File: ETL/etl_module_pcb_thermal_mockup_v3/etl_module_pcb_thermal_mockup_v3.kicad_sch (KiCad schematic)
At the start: 11 parts, among them J1 WP7B-S050VA1-R8000, J2 WP7B-S050VA1-R8000, J3 Conn_02x02_Odd_Even, J4 Conn_02x08_Counter_Clockwise, J5 Conn_02x08_Counter_Clockwise, J6 Conn_02x08_Counter_Clockwise, J7 Conn_02x08_Counter_Clockwise, X1 ETROC_dummy_thermal_sensors, X2 ETROC_dummy_thermal_sensors, X3 ETROC_dummy_thermal_sensors, X4 ETROC_dummy_thermal_sensors

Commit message: Progress on etl_module_pcb_thermal_mcokup_v3
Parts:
- J4, J5, J6, J7: symbol Connector_Generic:Conn_02x08_Counter_Clockwise -> Connector_Generic:Conn_02x08_Odd_Even
- U2: renamed from X2; footprint unl_silab:PCB_ETROC2_dummy -> (none)
- U3: renamed from X3; footprint unl_silab:PCB_ETROC2_dummy -> (none)
- U4: renamed from X4; footprint unl_silab:PCB_ETROC2_dummy -> (none)
- renumbered X1 to U1
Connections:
- net X1EBR2: now reaches J4.1 (Pin_1)
- net X1EBR2: now also U1.119 (ETROC_BR-)
- net X1LBL1: now reaches J4.10 (Pin_10)
- net X1LBL1: now also U1.11 (LGAD_BL+)
- net X1LBR1: now reaches J4.11 (Pin_11)
- net X1LBR1: now also U1.104 (LGAD_BR+)
- net X1LBL2: now reaches J4.12 (Pin_12)
- net X1LBL2: now also U1.12 (LGAD_BL-)
- net X1LTR2: now reaches J4.13 (Pin_13)
- net X1LTR2: now also U1.83 (LGAD_TR-)
- net X1LTL1: now reaches J4.14 (Pin_14)
- net X1LTL1: now also U1.21 (LGAD_TL+)
- net X1LTR1: now reaches J4.15 (Pin_15)
- net X1LTR1: now also U1.81 (LGAD_TR+)
- net X1LTL2: now reaches J4.16 (Pin_16)
- net X1LTL2: now also U1.23 (LGAD_TL-)
- net X1EBL1: now reaches J4.2 (Pin_2)
- net X1EBL1: now also U1.3 (ETROC_BLp)
- net X1EBR1: now reaches J4.3 (Pin_3)
- net X1EBR1: now also U1.117 (ETROC_BR+)
- net X1EBL2: now reaches J4.4 (Pin_4)
- net X1EBL2: now also U1.5 (ETROC_BL-)
- net X1ETR2: now reaches J4.5 (Pin_5)
- net X1ETR2: now also U1.108 (ETROC_TR-)
- net X1ETL1: now reaches J4.6 (Pin_6)
- net X1ETL1: now also U1.8 (ETROC_TL+)
- net X1ETR1: now reaches J4.7 (Pin_7)
- net X1ETR1: now also U1.107 (ETROC_TR+)
- net X1ETL2: now reaches J4.8 (Pin_8)
- net X1ETL2: now also U1.9 (ETROC_TL-)
- net X1LBR2: now reaches J4.9 (Pin_9)
- net X1LBR2: now also U1.105 (LGAD_BR-)
- net 01_N: no longer names the net of J2.1
- net 01_P: no longer names the net of J2.2
- net 02_N: no longer names the net of J2.3
- net 02_P: no longer names the net of J2.4
- net 03_N: no longer names the net of J2.5
- net 03_P: no longer names the net of J2.6
- net 04_N: no longer names the net of J2.7
- net 04_P: no longer names the net of J2.8
- net 05_N: no longer names the net of J2.9
- net 05_P: no longer names the net of J2.10
- net 06_N: no longer names the net of J2.11
- net 06_P: no longer names the net of J2.12
- net 07_N: no longer names the net of J2.13
- net 07_P: no longer names the net of J2.14
- net 08_N: no longer names the net of J2.15
- net 08_P: no longer names the net of J2.16
- net 09_N: no longer names the net of J2.17
- net 09_P: no longer names the net of J2.18
- net 10_N: no longer names the net of J2.19
- net 10_P: no longer names the net of J2.20
- net 11_N: no longer names the net of J2.21
- net 11_P: no longer names the net of J2.22
- net 12_N: no longer names the net of J2.23
- net 12_P: no longer names the net of J2.24
- net 13_N: no longer names the net of J2.25
- net 13_P: no longer names the net of J2.26
- net 14_N: no longer names the net of J2.27
- net 14_P: no longer names the net of J2.28
- net 15_N: no longer names the net of J2.29
- net 15_P: no longer names the net of J2.30
- net 16_N: no longer names the net of J2.31
- net 16_P: no longer names the net of J2.32
- net 17_N: no longer names the net of J2.33
- net 17_P: no longer names the net of J2.34
- net 18_N: no longer names the net of J2.35
- net 18_P: no longer names the net of J2.36
- net 19_N: no longer names the net of J2.37
- net 19_P: no longer names the net of J2.38
- net 20_N: no longer names the net of J2.39
- net 20_P: no longer names the net of J2.40
- net 21_N: no longer names the net of J2.41
- net 21_P: no longer names the net of J2.42
- net 22_N: no longer names the net of J2.43
- net 22_P: no longer names the net of J2.44
- net 23_N: no longer names the net of J2.45
- net 23_P: no longer names the net of J2.46
- net 24_N: no longer names the net of J2.47
- net 24_P: no longer names the net of J2.48
- net 26_N: no longer names the net of J1.2
- net 27_N: no longer names the net of J1.4
- net 27_P: no longer names the net of J1.3
- net 28_N: no longer names the net of J1.6
- net 28_P: no longer names the net of J1.5
- net 29_N: no longer names the net of J1.8
- net 29_P: no longer names the net of J1.7
- net 30_N: no longer names the net of J1.10
- net 30_P: no longer names the net of J1.9
- net 31_N: no longer names the net of J1.12
- net 31_P: no longer names the net of J1.11
- net 32_N: no longer names the net of J1.14
- net 32_P: no longer names the net of J1.13
- net 33_N: no longer names the net of J1.16
- net 33_P: no longer names the net of J1.15
- net 34_N: no longer names the net of J1.18
- net 34_P: no longer names the net of J1.17
- net 35_N: no longer names the net of J1.20
- net 35_P: no longer names the net of J1.19
- net 36_N: no longer names the net of J1.22
- net 36_P: no longer names the net of J1.21
- net 37_N: no longer names the net of J1.24
- net 37_P: no longer names the net of J1.23
- net 38_N: no longer names the net of J1.26
- net 38_P: no longer names the net of J1.25
- net 39_N: no longer names the net of J1.28
- net 39_P: no longer names the net of J1.27
- net 40_N: no longer names the net of J1.30
- net 40_P: no longer names the net of J1.29
- net 41_N: no longer names the net of J1.32
- net 41_P: no longer names the net of J1.31
- net 42_N: no longer names the net of J1.34
- net 42_P: no longer names the net of J1.33
- net 43_N: no longer names the net of J1.36
- net 43_P: no longer names the net of J1.35
- net 44_N: no longer names the net of J1.38
- net 44_P: no longer names the net of J1.37
- net 45_N: no longer names the net of J1.40
- net 45_P: no longer names the net of J1.39
- net 46_N: no longer names the net of J1.42
- net 46_P: no longer names the net of J1.41
- net 47_N: no longer names the net of J1.44
- net 47_P: no longer names the net of J1.43
- net 48_N: no longer names the net of J1.46
- net 48_P: no longer names the net of J1.45
- net 49_N: no longer names the net of J1.48
- net 49_P: no longer names the net of J1.47
- net S1: no longer names the net of J2.49
- net S1: no longer J2.50
- net S2: no longer names the net of J1.49
- net S2: no longer J1.50
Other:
- note added: "TODO: Wire up power to pin header Wire up power to b2b connector Wire up readout to pin header Wier up readout to b2b connector Add pin header for ETROC heater power supply"
- moved on the sheet: J4, J5, J6, J7

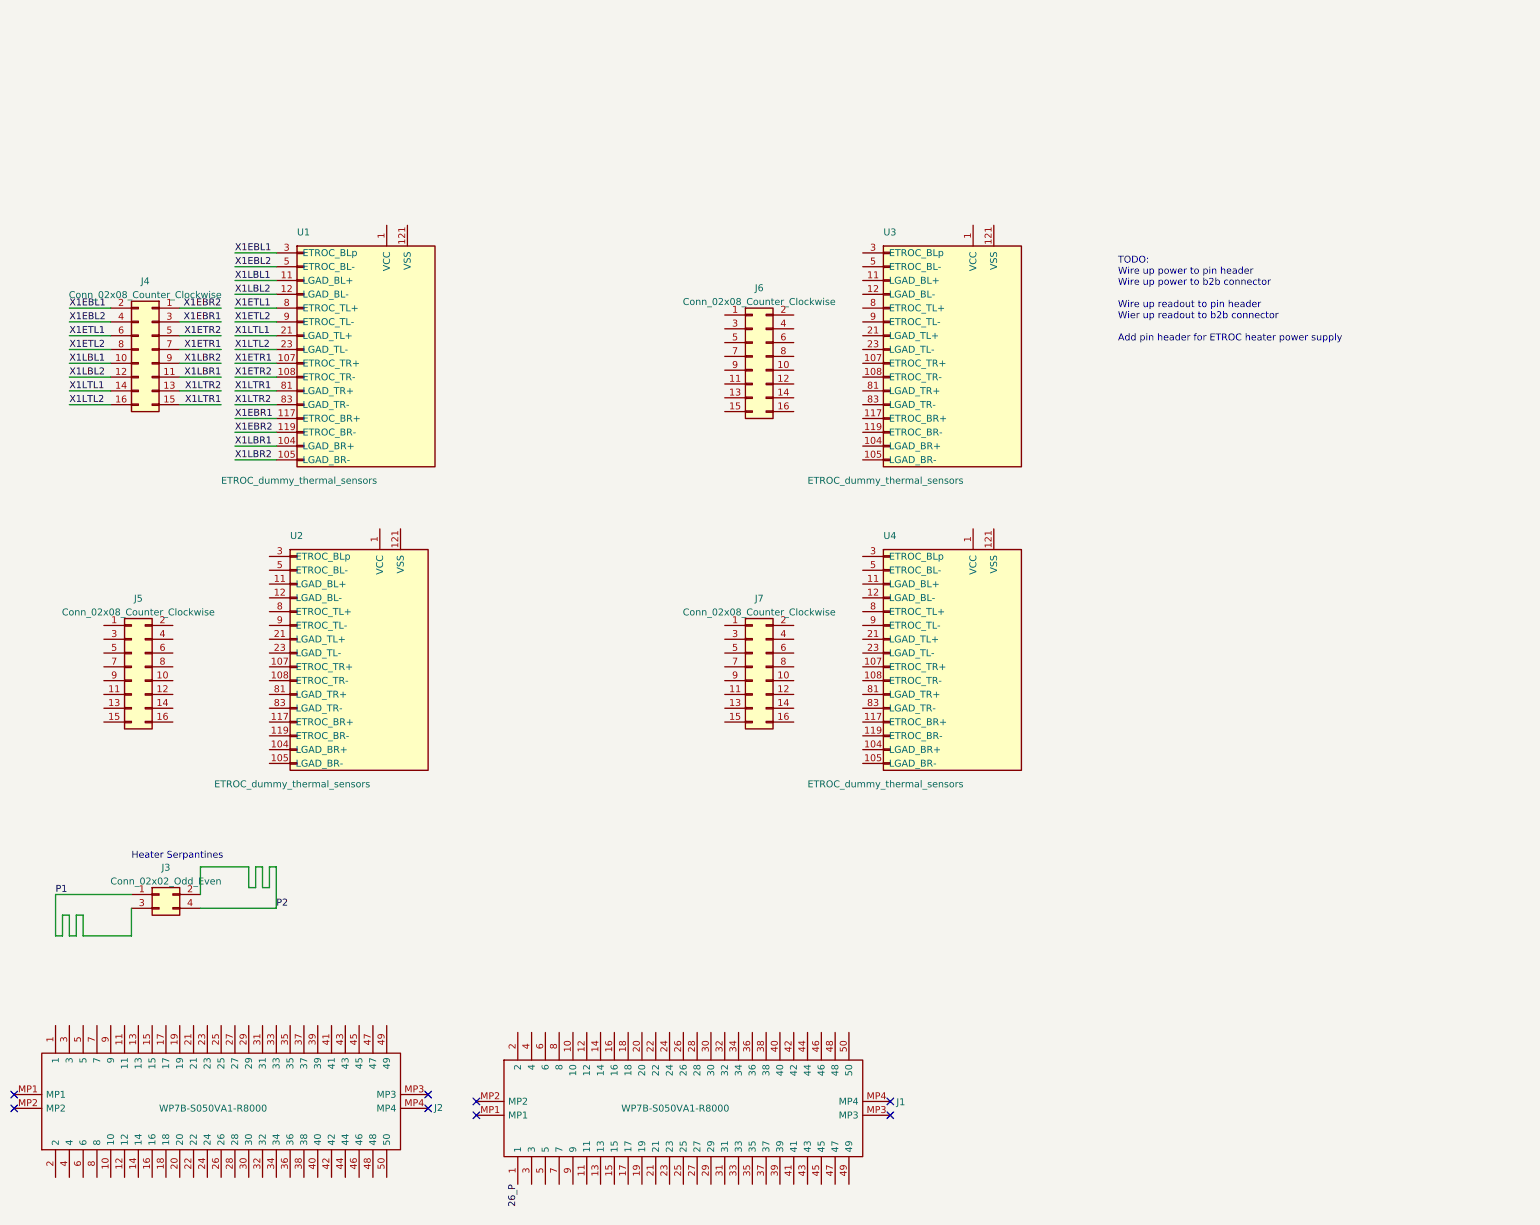
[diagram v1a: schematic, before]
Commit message: Finishes first draft of etl_module_pcb_thermal_mockup_v3
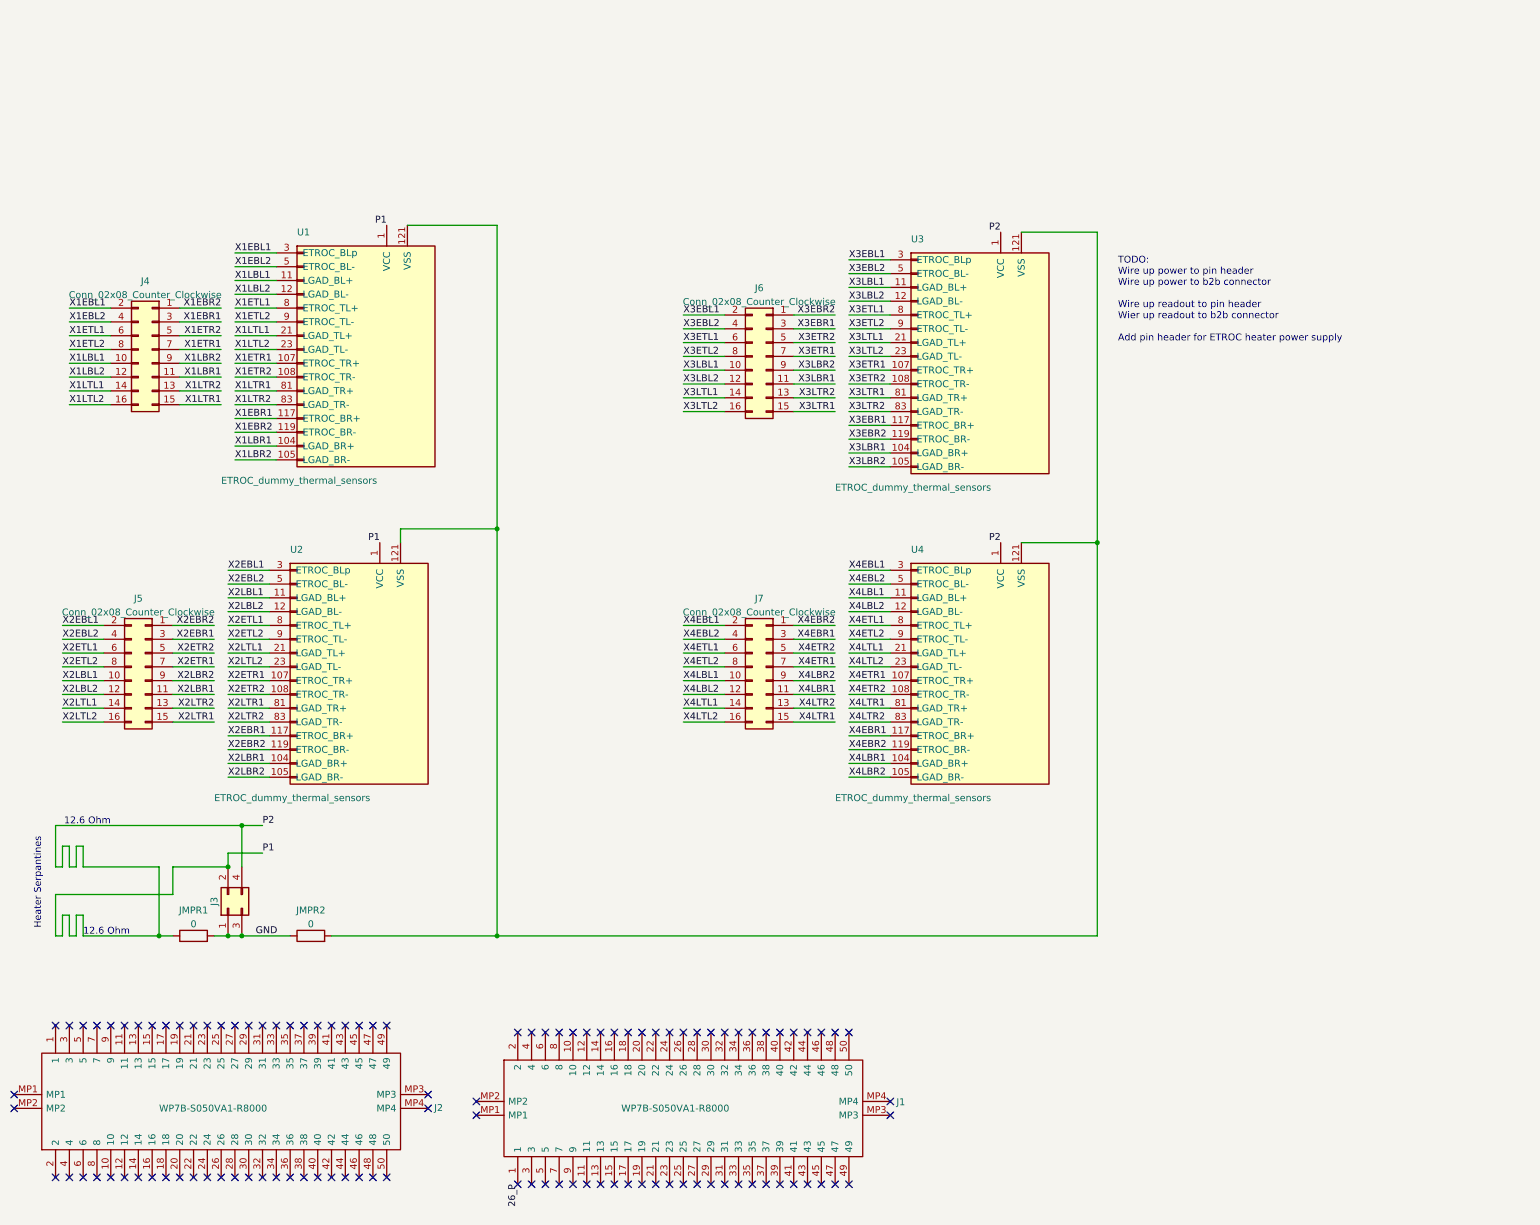
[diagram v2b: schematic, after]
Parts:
- added JMPR1, JMPR2: 0, Resistor_SMD:R_0805_2012Metric_Pad1.20x1.40mm_HandSolder, symbol Device:R
- U2, U3, U4: footprint (none) -> unl_silab:PCB_ETROC2_dummy
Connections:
- net P2 is gone; now on net P1: J3.2 (Pin_2), J3.4 (Pin_4)
- net P1: now also U1.1 (VCC), U2.1 (VCC), U3.1 (VCC), U4.1 (VCC), JMPR1.1; no longer J3.1 (Pin_1), J3.3 (Pin_3)
- net X3LBR1: now reaches U3.104 (LGAD_BR+)
- net X3LBR1: now also J6.11 (Pin_11)
- net X3LBR2: now reaches U3.105 (LGAD_BR-)
- net X3LBR2: now also J6.9 (Pin_9)
- net X3ETR1: now reaches U3.107 (ETROC_TR+)
- net X3ETR1: now also J6.7 (Pin_7)
- net X3ETR2: now reaches U3.108 (ETROC_TR-)
- net X3ETR2: now also J6.5 (Pin_5)
- net X3LBL1: now reaches U3.11 (LGAD_BL+)
- net X3LBL1: now also J6.10 (Pin_10)
- net X3EBR1: now reaches U3.117 (ETROC_BR+)
- net X3EBR1: now also J6.3 (Pin_3)
- net X3EBR2: now reaches U3.119 (ETROC_BR-)
- net X3EBR2: now also J6.1 (Pin_1)
- net X3LBL2: now reaches U3.12 (LGAD_BL-)
- net X3LBL2: now also J6.12 (Pin_12)
- net at U3.121 (VSS): now also U1.121 (VSS), U2.121 (VSS), U4.121 (VSS), JMPR2.2
- net X3LTL1: now reaches U3.21 (LGAD_TL+)
- net X3LTL1: now also J6.14 (Pin_14)
- net X3LTL2: now reaches U3.23 (LGAD_TL-)
- net X3LTL2: now also J6.16 (Pin_16)
- net X3EBL1: now reaches U3.3 (ETROC_BLp)
- net X3EBL1: now also J6.2 (Pin_2)
- net X3EBL2: now reaches U3.5 (ETROC_BL-)
- net X3EBL2: now also J6.4 (Pin_4)
- net X3ETL1: now reaches U3.8 (ETROC_TL+)
- net X3ETL1: now also J6.6 (Pin_6)
- net X3LTR1: now reaches U3.81 (LGAD_TR+)
- net X3LTR1: now also J6.15 (Pin_15)
- net X3LTR2: now reaches U3.83 (LGAD_TR-)
- net X3LTR2: now also J6.13 (Pin_13)
- net X3ETL2: now reaches U3.9 (ETROC_TL-)
- net X3ETL2: now also J6.8 (Pin_8)
- net X2EBR2: now reaches J5.1 (Pin_1)
- net X2EBR2: now also U2.119 (ETROC_BR-)
- net X2LBL1: now reaches J5.10 (Pin_10)
- net X2LBL1: now also U2.11 (LGAD_BL+)
- net X2LBR1: now reaches J5.11 (Pin_11)
- net X2LBR1: now also U2.104 (LGAD_BR+)
- net X2LBL2: now reaches J5.12 (Pin_12)
- net X2LBL2: now also U2.12 (LGAD_BL-)
- net X2LTR2: now reaches J5.13 (Pin_13)
- net X2LTR2: now also U2.83 (LGAD_TR-)
- net X2LTL1: now reaches J5.14 (Pin_14)
- net X2LTL1: now also U2.21 (LGAD_TL+)
- net X2LTR1: now reaches J5.15 (Pin_15)
- net X2LTR1: now also U2.81 (LGAD_TR+)
- net X2LTL2: now reaches J5.16 (Pin_16)
- net X2LTL2: now also U2.23 (LGAD_TL-)
- net X2EBL1: now reaches J5.2 (Pin_2)
- net X2EBL1: now also U2.3 (ETROC_BLp)
- net X2EBR1: now reaches J5.3 (Pin_3)
- net X2EBR1: now also U2.117 (ETROC_BR+)
- net X2EBL2: now reaches J5.4 (Pin_4)
- net X2EBL2: now also U2.5 (ETROC_BL-)
- net X2ETR2: now reaches J5.5 (Pin_5)
- net X2ETR2: now also U2.108 (ETROC_TR-)
- net X2ETL1: now reaches J5.6 (Pin_6)
- net X2ETL1: now also U2.8 (ETROC_TL+)
- net X2ETR1: now reaches J5.7 (Pin_7)
- net X2ETR1: now also U2.107 (ETROC_TR+)
- net X2ETL2: now reaches J5.8 (Pin_8)
- net X2ETL2: now also U2.9 (ETROC_TL-)
- net X2LBR2: now reaches J5.9 (Pin_9)
- net X2LBR2: now also U2.105 (LGAD_BR-)
- net X4LBR1: now reaches U4.104 (LGAD_BR+)
- net X4LBR1: now also J7.11 (Pin_11)
- net X4LBR2: now reaches U4.105 (LGAD_BR-)
- net X4LBR2: now also J7.9 (Pin_9)
- net X4ETR1: now reaches U4.107 (ETROC_TR+)
- net X4ETR1: now also J7.7 (Pin_7)
- net X4ETR2: now reaches U4.108 (ETROC_TR-)
- net X4ETR2: now also J7.5 (Pin_5)
- net X4LBL1: now reaches U4.11 (LGAD_BL+)
- net X4LBL1: now also J7.10 (Pin_10)
- net X4EBR1: now reaches U4.117 (ETROC_BR+)
- net X4EBR1: now also J7.3 (Pin_3)
- net X4EBR2: now reaches U4.119 (ETROC_BR-)
- net X4EBR2: now also J7.1 (Pin_1)
- net X4LBL2: now reaches U4.12 (LGAD_BL-)
- net X4LBL2: now also J7.12 (Pin_12)
- net X4LTL1: now reaches U4.21 (LGAD_TL+)
- net X4LTL1: now also J7.14 (Pin_14)
- net X4LTL2: now reaches U4.23 (LGAD_TL-)
- net X4LTL2: now also J7.16 (Pin_16)
- net X4EBL1: now reaches U4.3 (ETROC_BLp)
- net X4EBL1: now also J7.2 (Pin_2)
- net X4EBL2: now reaches U4.5 (ETROC_BL-)
- net X4EBL2: now also J7.4 (Pin_4)
- net X4ETL1: now reaches U4.8 (ETROC_TL+)
- net X4ETL1: now also J7.6 (Pin_6)
- net X4LTR1: now reaches U4.81 (LGAD_TR+)
- net X4LTR1: now also J7.15 (Pin_15)
- net X4LTR2: now reaches U4.83 (LGAD_TR-)
- net X4LTR2: now also J7.13 (Pin_13)
- net X4ETL2: now reaches U4.9 (ETROC_TL-)
- net X4ETL2: now also J7.8 (Pin_8)
- new net GND: J3.1 (Pin_1), J3.3 (Pin_3), JMPR1.2, JMPR2.1
- no-connect marks 8 -> 108
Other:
- note added: "12.6 Ohm"
- moved on the sheet: J3, U2, U3, U4
